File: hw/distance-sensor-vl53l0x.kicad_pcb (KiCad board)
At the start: 2 copper layers, 24 x 24 mm, 32 parts, among them J1 DFU, J2 USB_OTG, J3 CONN_02X05, J4 UART, U1 STM32F042F6Px, U2 MIC5504-3.3, U3 VL53L0X, U4 MIC5504-2.8

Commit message: Hardware changes for rev2
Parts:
- removed C8: 1uF, Capacitors_SMD:C_0603
- removed D1: LED, LEDs:LED_0603
- removed R5: 220R, Resistors_SMD:R_0603
- removed REF** (x2): MountingHole_3.2mm_M3, Mounting_Holes:MountingHole_3.2mm_M3
- removed U4: MIC5504-2.8, TO_SOT_Packages_SMD:SOT-23-5
- added J101: TEST_1P, mounting_hole:Mounting_hole_3mm, F.Cu at (96.0, 99.8)
- added J102: TEST_1P, mounting_hole:Mounting_hole_3mm, F.Cu at (116.0, 99.8)
- moved C5 7.62 mm to (113.6, 103.2)
- moved U2 7.38 mm to (113.6, 106.0)
- moved R3 7.25 mm to (107.0, 107.2)
- moved R4 7.25 mm to (105.2, 107.2)
- moved J2 7.25 mm to (106.1, 111.2)
- moved C2 6.83 mm to (113.5, 108.8)
- moved R6 4.50 mm to (113.2, 92.0)
- moved R12 1.90 mm to (99.5, 109.2), turned to 180 degrees
- moved D2 1.51 mm to (113.2, 93.5), turned to 180 degrees
- moved J1 1.25 mm to (97.8, 94.2), turned to 180 degrees
- moved R11 1.03 mm to (99.5, 107.5), turned to 180 degrees
- moved R1 0.48 mm to (97.8, 96.3)
- moved J4 0.39 mm to (96.2, 111.8), turned to 180 degrees
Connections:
- C6 pad 1: +2.8V -> +3.3V
- C7 pad 1: +2.8V -> +3.3V
- J1 pad 1: GND -> /BOOT0
- J1 pad 2: /BOOT0 -> +3.3V
- J2 pad 4: (no net) -> Net-(J2-Pad4)
- J3 pad 6: (no net) -> /SWO
- J3 pad 8: (no net) -> Net-(J3-Pad8)
- R10 pad 1: +2.8V -> +3.3V
- R7 pad 1: +2.8V -> +3.3V
- R8 pad 1: +2.8V -> +3.3V
- R9 pad 1: +2.8V -> +3.3V
- U1 pad 14: (no net) -> Net-(U1-Pad14)
- U1 pad 6: (no net) -> Net-(U1-Pad6)
- U1 pad 7: (no net) -> /USART_DE
- U2 pad 3: (no net) -> +5V
- U3 pad 1: +2.8V -> +3.3V
- U3 pad 11: +2.8V -> +3.3V
- U3 pad 8: (no net) -> Net-(U3-Pad8)
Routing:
- net +2.8V: track 30.1 -> 0.00 mm, vias 6 -> 0
- net GND: track 90.9 -> 75.3 mm, vias 6 -> 7
- net Net-(U1-Pad10): track 11.4 -> 0.00 mm, vias 2 -> 0
- net +3.3V: track 63.5 -> 71.4 mm, vias 6 -> 11
- net +5V: track 22.7 -> 28.2 mm, vias 1 -> 2
- net /USB_D_P: track 19.5 -> 24.1 mm, vias 0 -> 2
- net /USB_D_N: track 18.9 -> 23.3 mm, vias 2 -> 0
- net Net-(R6-Pad2): track 6.36 -> 9.83 mm
- net /USART_TX: track 19.7 -> 21.7 mm
- net Net-(D1-Pad1): track 1.56 -> 0.00 mm
- net Net-(J4-Pad2): track 3.16 -> 2.50 mm
- net Net-(D2-Pad1): track 2.06 -> 1.52 mm
- net Net-(J4-Pad3): track 3.47 -> 2.94 mm
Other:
- net class Default: clearance 0.2 -> 0
- rule trace_clearance: 0.2 -> 0
- board text added: "3.3V UART"
- board text added: "DFU"
- board text added: "VCC"
- board text added: "rev2"
- board text removed: "3.3-5.5V in 3.3V IO"
- board text removed: "V+"

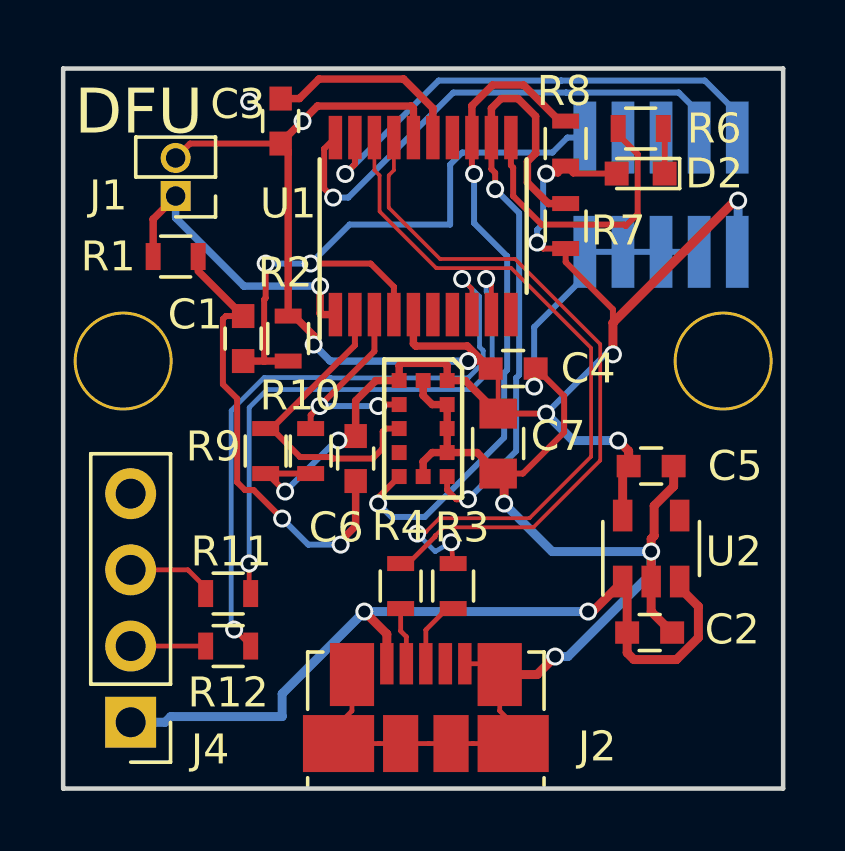
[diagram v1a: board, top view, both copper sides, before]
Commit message: Change PCB corners to rounded.
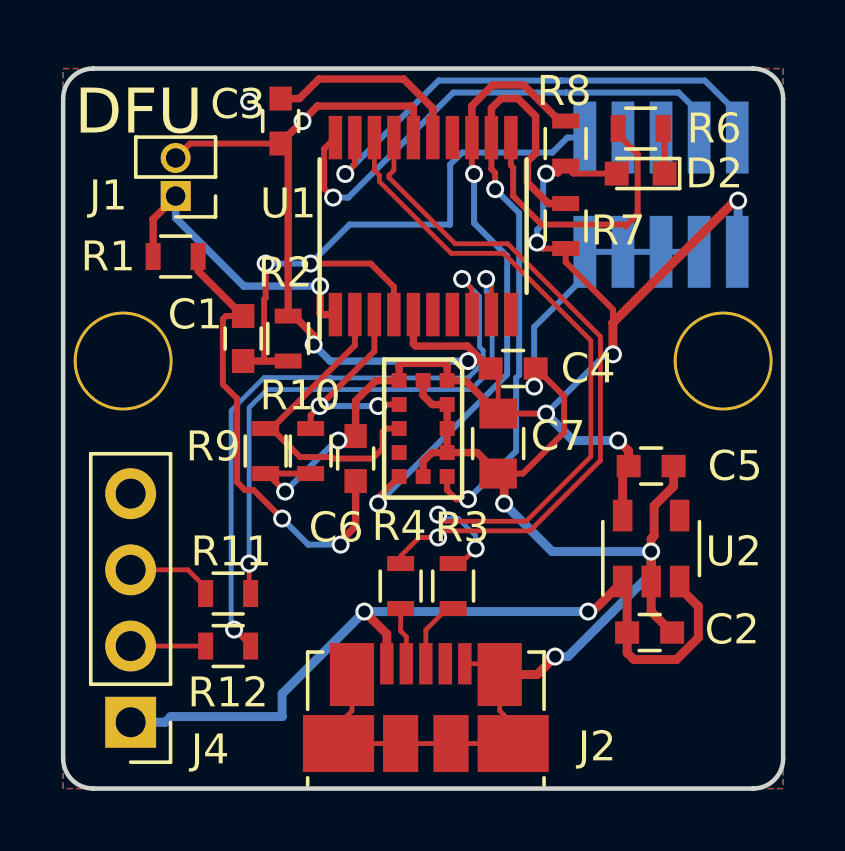
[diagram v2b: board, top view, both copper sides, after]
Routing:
- net /I2C_INT: track 22.2 -> 20.6 mm
- net /USB_D_N: track 23.3 -> 22.8 mm, vias 0 -> 1
- net /USB_D_P: track 24.1 -> 23.6 mm
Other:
- outline, holes or cut-outs redrawn
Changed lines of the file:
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@@
-(kicad_pcb (version 20170123) (host pcbnew "(2017-08-19 revision a20cce075)-master")
+(kicad_pcb (version 20170123) (host pcbnew "(2017-08-16 revision 90873a101)-master")
   (general
     (thickness 1.6)
-    (drawings 15)
-    (tracks 375)
+    (drawings 19)
+    (tracks 371)
     (zones 0)
     (modules 28)
@@
   )
   (setup
-    (last_trace_width 0.16)
+    (last_trace_width 0.2)
     (user_trace_width 0.16)
     (trace_clearance 0)
@@
     )
   )
+  (gr_arc (start 117 113) (end 117 114) (angle -90) (layer Edge.Cuts) (width 0.15))
+  (gr_arc (start 117 91) (end 118 91) (angle -90) (layer Edge.Cuts) (width 0.15))
+  (gr_arc (start 95 91) (end 95 90) (angle -90) (layer Edge.Cuts) (width 0.15))
+  (gr_arc (start 95 113) (end 94 113) (angle -90) (layer Edge.Cuts) (width 0.15))
   (dimension 24 (width 0.3) (layer Eco2.User)
     (gr_text "24,000 mm" (at 106 118.55) (layer Eco2.User)
@@
     (effects (font (size 1.5 1.5) (thickness 0.3)) (justify mirror))
   )
-  (gr_line (start 94 90) (end 94 114) (layer Edge.Cuts) (width 0.15))
-  (gr_line (start 118 90) (end 94 90) (layer Edge.Cuts) (width 0.15))
-  (gr_line (start 118 114) (end 118 90) (layer Edge.Cuts) (width 0.15))
-  (gr_line (start 94 114) (end 118 114) (layer Edge.Cuts) (width 0.15))
+  (gr_line (start 94 91) (end 94 113) (layer Edge.Cuts) (width 0.15))
+  (gr_line (start 117 90) (end 95 90) (layer Edge.Cuts) (width 0.15))
+  (gr_line (start 118 113) (end 118 91) (layer Edge.Cuts) (width 0.15))
+  (gr_line (start 95 114) (end 117 114) (layer Edge.Cuts) (width 0.15))
   (segment (start 101.5 99.75) (end 100.7 99.75) (width 0.25) (layer F.Cu) (net 1) (status 10))
   (segment (start 100.7 99.75) (end 100 99.75) (width 0.25) (layer F.Cu) (net 1) (status 20))
@@
   (segment (start 107.625 97.34) (end 107.3 97.015) (width 0.16) (layer F.Cu) (net 16))
   (via (at 107.3 97.015) (size 0.6) (drill 0.4) (layers F.Cu B.Cu) (net 16))
+  (segment (start 107.697862 93.939087) (end 107.697862 93.514823) (width 0.2) (layer B.Cu) (net 18))
+  (segment (start 107.697862 95.151564) (end 107.697862 93.939087) (width 0.2) (layer B.Cu) (net 18))
+  (segment (start 108.799987 96.253689) (end 107.697862 95.151564) (width 0.2) (layer B.Cu) (net 18))
+  (segment (start 108.799987 100.200013) (end 108.799987 96.253689) (width 0.2) (layer B.Cu) (net 18))
+  (segment (start 104.5 104.5) (end 108.799987 100.200013) (width 0.2) (layer B.Cu) (net 18))
   (segment (start 102.700001 94.000001) (end 102.700001 92.674999) (width 0.2) (layer F.Cu) (net 19))
   (segment (start 103 94.3) (end 102.700001 94.000001) (width 0.2) (layer F.Cu) (net 19))
@@
   (segment (start 109.75 92.824998) (end 109.75 91.589998) (width 0.25) (layer F.Cu) (net 17))
   (via (at 108.400843 94.019283) (size 0.6) (drill 0.4) (layers F.Cu B.Cu) (net 17))
-  (segment (start 107.697862 95.151564) (end 107.697862 93.514823) (width 0.2) (layer B.Cu) (net 18))
-  (segment (start 104.5 104.5) (end 104.946142 104.946142) (width 0.2) (layer B.Cu) (net 18))
-  (segment (start 104.946142 104.946142) (end 106.053858 104.946142) (width 0.2) (layer B.Cu) (net 18))
-  (segment (start 108.799987 96.253689) (end 107.697862 95.151564) (width 0.2) (layer B.Cu) (net 18))
-  (segment (start 108.799987 100.046309) (end 108.799987 96.253689) (width 0.2) (layer B.Cu) (net 18))
-  (segment (start 108.699987 100.146309) (end 108.799987 100.046309) (width 0.2) (layer B.Cu) (net 18))
-  (segment (start 106.053858 104.946142) (end 108.699987 102.300013) (width 0.2) (layer B.Cu) (net 18))
-  (segment (start 108.699987 102.300013) (end 108.699987 100.146309) (width 0.2) (layer B.Cu) (net 18))
   (segment (start 107.625 93.441961) (end 107.697862 93.514823) (width 0.2) (layer F.Cu) (net 18))
   (segment (start 107.625 92.3) (end 107.625 93.441961) (width 0.2) (layer F.Cu) (net 18) (status 10))
@@
   (segment (start 110.55 91.75) (end 109.349989 90.549989) (width 0.25) (layer F.Cu) (net 18) (status 10))
   (segment (start 110.75 91.75) (end 110.55 91.75) (width 0.25) (layer F.Cu) (net 18) (status 30))
-  (via (at 106.934 105.791) (size 0.6) (drill 0.4) (layers F.Cu B.Cu) (net 20))
-  (segment (start 106.934 105.791) (end 107 106.5) (width 0.16) (layer F.Cu) (net 20))
-  (segment (start 106.934 105.791) (end 106.4 106.1) (width 0.16) (layer B.Cu) (net 20))
-  (segment (start 106.4 106.1) (end 105.8 105.5) (width 0.16) (layer B.Cu) (net 20))
-  (segment (start 106.0975 105.436832) (end 105.863168 105.436832) (width 0.16) (layer F.Cu) (net 20))
-  (segment (start 104.375 93.387501) (end 104.5475 93.560001) (width 0.125) (layer F.Cu) (net 20))
-  (segment (start 104.375 92.3) (end 104.375 93.387501) (width 0.125) (layer F.Cu) (net 20) (status 10))
-  (segment (start 104.5475 93.560001) (end 104.5475 94.763168) (width 0.125) (layer F.Cu) (net 20))
-  (segment (start 104.5475 94.763168) (end 106.436832 96.6525) (width 0.125) (layer F.Cu) (net 20))
-  (segment (start 106.436832 96.6525) (end 108.936832 96.6525) (width 0.125) (layer F.Cu) (net 20))
-  (segment (start 108.936832 96.6525) (end 111.5975 99.313168) (width 0.125) (layer F.Cu) (net 20))
-  (segment (start 111.5975 99.313168) (end 111.5975 102.936832) (width 0.125) (layer F.Cu) (net 20))
-  (segment (start 111.5975 102.936832) (end 109.545397 104.988935) (width 0.125) (layer F.Cu) (net 20))
-  (segment (start 109.545397 104.988935) (end 106.545397 104.988935) (width 0.125) (layer F.Cu) (net 20))
-  (segment (start 106.545397 104.988935) (end 106.0975 105.436832) (width 0.125) (layer F.Cu) (net 20))
-  (via (at 105.8 105.5) (size 0.6) (drill 0.4) (layers F.Cu B.Cu) (net 20))
-  (segment (start 105.863168 105.436832) (end 105.8 105.5) (width 0.16) (layer F.Cu) (net 20))
-  (segment (start 106.4 105.565668) (end 106.4 105.6) (width 0.16) (layer F.Cu) (net 21))
-  (segment (start 106.4 105.6) (end 105.5 106.5) (width 0.16) (layer F.Cu) (net 21) (status 800020))
-  (segment (start 105.5 106.5) (end 105.25 106.5) (width 0.16) (layer F.Cu) (net 21) (status C00030))
-  (segment (start 106.671733 105.293935) (end 106.4 105.565668) (width 0.125) (layer F.Cu) (net 21))
-  (segment (start 106.4 105.565668) (end 106.4025 105.563168) (width 0.125) (layer F.Cu) (net 21))
-  (segment (start 105.025 93.387501) (end 104.8525 93.560001) (width 0.125) (layer F.Cu) (net 21))
-  (segment (start 105.025 92.3) (end 105.025 93.387501) (width 0.125) (layer F.Cu) (net 21) (status 10))
-  (segment (start 104.8525 93.560001) (end 104.8525 94.636832) (width 0.125) (layer F.Cu) (net 21))
-  (segment (start 104.8525 94.636832) (end 106.563168 96.3475) (width 0.125) (layer F.Cu) (net 21))
-  (segment (start 106.563168 96.3475) (end 109.063168 96.3475) (width 0.125) (layer F.Cu) (net 21))
-  (segment (start 109.063168 96.3475) (end 111.9025 99.186832) (width 0.125) (layer F.Cu) (net 21))
-  (segment (start 111.9025 99.186832) (end 111.9025 103.063168) (width 0.125) (layer F.Cu) (net 21))
-  (segment (start 111.9025 103.063168) (end 109.671733 105.293935) (width 0.125) (layer F.Cu) (net 21))
-  (segment (start 109.671733 105.293935) (end 106.671733 105.293935) (width 0.125) (layer F.Cu) (net 21))
+  (segment (start 107.75 106) (end 107.75 105.575736) (width 0.16) (layer B.Cu) (net 20))
+  (segment (start 107.75 105.575736) (end 107.174264 105) (width 0.16) (layer B.Cu) (net 20))
+  (segment (start 107.174264 105) (end 106.5 105) (width 0.16) (layer B.Cu) (net 20))
+  (segment (start 107 106.5) (end 107.25 106.5) (width 0.16) (layer F.Cu) (net 20))
+  (segment (start 107.25 106.5) (end 107.75 106) (width 0.16) (layer F.Cu) (net 20))
+  (via (at 107.75 106) (size 0.6) (drill 0.4) (layers F.Cu B.Cu) (net 20))
+  (via (at 106.5 104.87) (size 0.6) (drill 0.4) (layers F.Cu B.Cu) (net 20))
+  (segment (start 106.72 105.09) (end 106.5 104.87) (width 0.16) (layer F.Cu) (net 20))
+  (segment (start 109.433724 105.09) (end 106.72 105.09) (width 0.16) (layer F.Cu) (net 20))
+  (segment (start 111.59 102.933724) (end 109.433724 105.09) (width 0.16) (layer F.Cu) (net 20))
+  (segment (start 111.59 99.066276) (end 111.59 102.933724) (width 0.16) (layer F.Cu) (net 20))
+  (segment (start 108.683724 96.16) (end 111.59 99.066276) (width 0.16) (layer F.Cu) (net 20))
+  (segment (start 106.933724 96.16) (end 108.683724 96.16) (width 0.16) (layer F.Cu) (net 20))
+  (segment (start 104.54 93.766276) (end 106.933724 96.16) (width 0.16) (layer F.Cu) (net 20))
+  (segment (start 104.375 92.3) (end 104.375 93.387501) (width 0.16) (layer F.Cu) (net 20))
+  (segment (start 104.375 93.387501) (end 104.54 93.552501) (width 0.16) (layer F.Cu) (net 20))
+  (segment (start 104.54 93.552501) (end 104.54 93.766276) (width 0.16) (layer F.Cu) (net 20))
+  (segment (start 106.5 105.63) (end 105.87 105.63) (width 0.16) (layer F.Cu) (net 21))
+  (segment (start 105.87 105.63) (end 105.25 106.25) (width 0.16) (layer F.Cu) (net 21))
+  (segment (start 109.566276 105.41) (end 106.72 105.41) (width 0.16) (layer F.Cu) (net 21))
+  (via (at 106.5 105.63) (size 0.6) (drill 0.4) (layers F.Cu B.Cu) (net 21))
+  (segment (start 106.72 105.41) (end 106.5 105.63) (width 0.16) (layer F.Cu) (net 21))
+  (segment (start 111.91 103.066276) (end 109.566276 105.41) (width 0.16) (layer F.Cu) (net 21))
+  (segment (start 111.91 98.933724) (end 111.91 103.066276) (width 0.16) (layer F.Cu) (net 21))
+  (segment (start 108.816276 95.84) (end 111.91 98.933724) (width 0.16) (layer F.Cu) (net 21))
+  (segment (start 107.066276 95.84) (end 108.816276 95.84) (width 0.16) (layer F.Cu) (net 21))
+  (segment (start 104.86 93.633724) (end 107.066276 95.84) (width 0.16) (layer F.Cu) (net 21))
+  (segment (start 105.025 92.3) (end 105.025 93.387501) (width 0.16) (layer F.Cu) (net 21))
+  (segment (start 105.025 93.387501) (end 104.86 93.552501) (width 0.16) (layer F.Cu) (net 21))
+  (segment (start 104.86 93.552501) (end 104.86 93.633724) (width 0.16) (layer F.Cu) (net 21))
   (zone (net 2) (net_name GND) (layer F.Cu) (hatch edge 0.508)
     (connect_pads (clearance 0.508))
